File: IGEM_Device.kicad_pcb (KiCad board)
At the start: 2 copper layers, 50.2 x 47.6 mm, 28 parts, among them J1 67997-410HLF, J2 Electrode_Conn, J3 Batt_Conn, SW1 Power_Switch, U1 SaBLE-X-R2, U2 TC1014-2.85VCT713, U3 LMP91000SD_NOPB, U4 LM334MX_NOPB, U5 TPS79718QDCKRQ1, U6 G-NIMO-003

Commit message: Update to PCB and Gerber files
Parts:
- moved J2 1.91 mm to (125.1, 47.6)
- moved U3 1.91 mm to (125.1, 59.7)
- moved R1 1.42 mm to (144.8, 81.9)
- moved R2 1.42 mm to (141.6, 81.9)
- moved D1 1.27 mm to (137.2, 52.1)
- moved J3 1.27 mm to (109.9, 94.6)
- moved R5 0.64 mm to (135.9, 55.2)
- moved U4 0.64 mm to (145.4, 54.0)
- moved U1 0.64 mm to (131.4, 71.1)
- moved R3 0.63 mm to (138.4, 55.2)
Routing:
- net +2V85: track 99.5 -> 117.1 mm, vias 1 -> 3
- net /TEMP_OUT: track 29.3 -> 36.2 mm
- net +1V8: track 35.3 -> 30.8 mm
- net /EXT_TEMP_SCL: track 73.5 -> 69.7 mm
- net /IP_CONTROL: track 35.7 -> 37.5 mm
- net /JTAG_TDO: track 14.5 -> 12.9 mm
- net Net-(D1-PadA): track 6.65 -> 8.16 mm
- net +BATT: track 44.7 -> 45.7 mm
- net /EXT_TEMP_SDA: track 93.0 -> 92.1 mm
- net GND: track 212.3 -> 213.1 mm
- net /IP_CATHODE: track 8.09 -> 8.77 mm
- net /RESET: track 5.44 -> 6.08 mm
- net /JTAG_TMSC: track 4.17 -> 4.80 mm
- net /JTAG_TCXC: track 4.81 -> 5.44 mm
- net /POWER_GOOD: track 43.3 -> 44.0 mm
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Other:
- board size 50.2 x 47.6 mm -> 50.2 x 47 mm

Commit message: Minor changes
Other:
- rule via_min_size: 0.4 -> 0.5

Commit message: Minor fixes
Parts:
- removed C9: 0.1u, Capacitors_SMD:C_0805
- removed SW1: Power_Switch, footprints5:JS202011SCQN
- added C13: 100p, Capacitors_SMD:C_0805, F.Cu at (154.3, 93.3)
- added J4: Male_Data_Conn, HTSW10407GS:HTSW-104-07-G-S, F.Cu at (157.5, 54.0)
- added J5: Female_Data_Conn, 55342372:5-534237-2, B.Cu at (161.3, 83.2)
- added J6: VDD_Female_Conn, 55342371:5-534237-1, F.Cu at (141.6, 97.8)
- added J7: GND_Female_Conn, 55342371:5-534237-1, F.Cu at (173.4, 97.8)
- added J8: VDD_Male_Conn, 51462803:5-146280-3, F.Cu at (141.6, 63.5)
- added J9: GND_Male_Conn, 51462803:5-146280-3, F.Cu at (173.4, 63.5)
- added U7: ADS1100A0IDBVR, ADS1100A0TDBVR:ADS1100A0IDBVR, F.Cu at (154.3, 90.2)
- C3: moved to B.Cu
- D1: footprint SODFL1608X70N -> 1N4148WT:SODFL1608X70N
- J1: value 67997-410HLF -> M20-9980445; footprint footprints3:67997-410HLF -> M20-9980445:HDRV8W64P254_2X4_1016X508X910P
- J3: footprint footprints6:796136-1 -> S2B-PH-K-S_LF__SN_:JST_S2B-PH-K-S(LF)(SN)
- U6: moved to F.Cu
- moved R4 69.9 mm to (167.6, 83.8)
- moved U5 69.6 mm to (167.6, 86.4)
- moved C5 69.0 mm to (170.8, 83.8), turned to 270 degrees
- moved C4 68.7 mm to (170.8, 87.6), turned to 90 degrees
- moved C6 66.1 mm to (167.6, 89.5), turned to 0 degrees
- moved J2 63.5 mm to (157.5, 102.2), turned to 180 degrees
- moved U6 62.3 mm to (168.3, 96.5), turned to 270 degrees
- moved C11 52.3 mm to (142.9, 54.0)
- moved C10 50.2 mm to (170.2, 66.0), turned to 0 degrees
- moved J3 47.3 mm to (141.0, 59.1), turned to 90 degrees
- moved U3 46.8 mm to (160.7, 90.2), turned to 270 degrees
- moved D1 44.4 mm to (147.3, 95.2), turned to 180 degrees
- moved C7 44.0 mm to (170.2, 63.5), turned to 0 degrees
- moved U2 41.6 mm to (146.7, 54.0)
- moved J1 41.0 mm to (172.7, 52.7), turned to 270 degrees
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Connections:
- C12 pad 1: +3V3 -> +2V85
- C3 pad 1: Net-(C3-Pad1) -> +BATT
- J1 pad 1: +3V3 -> GND
- J1 pad 2: GND -> /RESET
- J1 pad 4: Net-(J1-Pad4) -> /JTAG_TCXC
- J1 pad 5: GND -> /JTAG_TDI
- J1 pad 6: /RESET -> /JTAG_TMSC
- J1 pad 7: /JTAG_TCXC -> /JTAG_TDO
- J1 pad 8: /JTAG_TMSC -> +2V85
- R1 pad 2: /EXT_TEMP_SDA -> /SCL
- R2 pad 2: /EXT_TEMP_SCL -> /SDA
- U1 pad 17: /IP_CONTROL -> Net-(U1-Pad17)
- U1 pad 21: /POWER_GOOD -> Net-(U1-Pad21)
- U1 pad 24: /TEMP_OUT -> Net-(U1-Pad24)
- U1 pad 29: Net-(U1-Pad29) -> /POWER_GOOD
- U1 pad 30: Net-(U1-Pad30) -> /IP_CONTROL
- U1 pad 31: /EXT_TEMP_SCL -> /SDA
- U1 pad 32: /EXT_TEMP_SDA -> /SCL
- U2 pad 1: Net-(C3-Pad1) -> +BATT
- U2 pad 3: Net-(C3-Pad1) -> +BATT
- U3 pad 3: /EXT_TEMP_SCL -> /SCL
- U3 pad 4: /EXT_TEMP_SDA -> /SDA
- U3 pad 8: /TEMP_OUT -> /LMP91000_VOUT
- U6 pad 2: /EXT_TEMP_SCL -> /SCL
- U6 pad 3: /EXT_TEMP_SDA -> /SDA
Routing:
- net /EXT_TEMP_SDA: track 92.1 -> 0.00 mm, vias 3 -> 0
- net /EXT_TEMP_SCL: track 69.7 -> 0.00 mm, vias 3 -> 0
- net /SCL: track 0.00 -> 42.2 mm, vias 0 -> 3
- net /TEMP_OUT: track 36.2 -> 0.00 mm, vias 2 -> 0
- net +BATT: track 45.7 -> 12.0 mm
- net /SDA: track 0.00 -> 32.9 mm, vias 0 -> 2
- net /POWER_GOOD: track 44.0 -> 13.4 mm, vias 2 -> 0
- net Net-(C3-Pad1): track 27.7 -> 0.00 mm
- net GND: track 213.5 -> 194.1 mm, vias 1 -> 3
- net /IP_CONTROL: track 37.5 -> 19.9 mm, vias 2 -> 0
- net /RESET: track 6.08 -> 23.1 mm, vias 0 -> 1
- net /JTAG_TCXC: track 5.44 -> 19.9 mm, vias 0 -> 1
- net /JTAG_TMSC: track 4.80 -> 16.9 mm, vias 0 -> 1
- net Net-(C1-Pad1): track 3.75 -> 12.8 mm
- net +1V8: track 30.8 -> 39.6 mm, vias 2 -> 4
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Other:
- board size 50.2 x 47 mm -> 35.6 x 47.6 mm

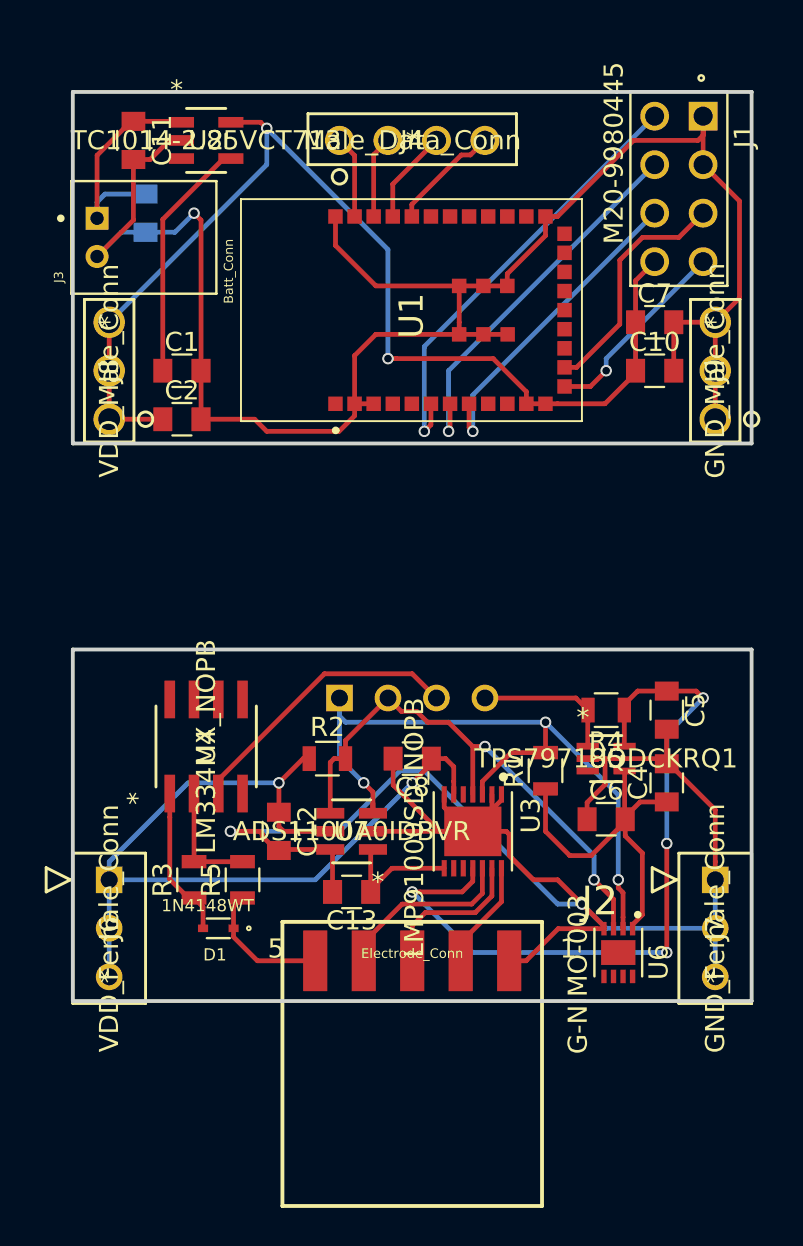
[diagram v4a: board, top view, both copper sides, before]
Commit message: Updated layout, added 3D shapes and Gerber files
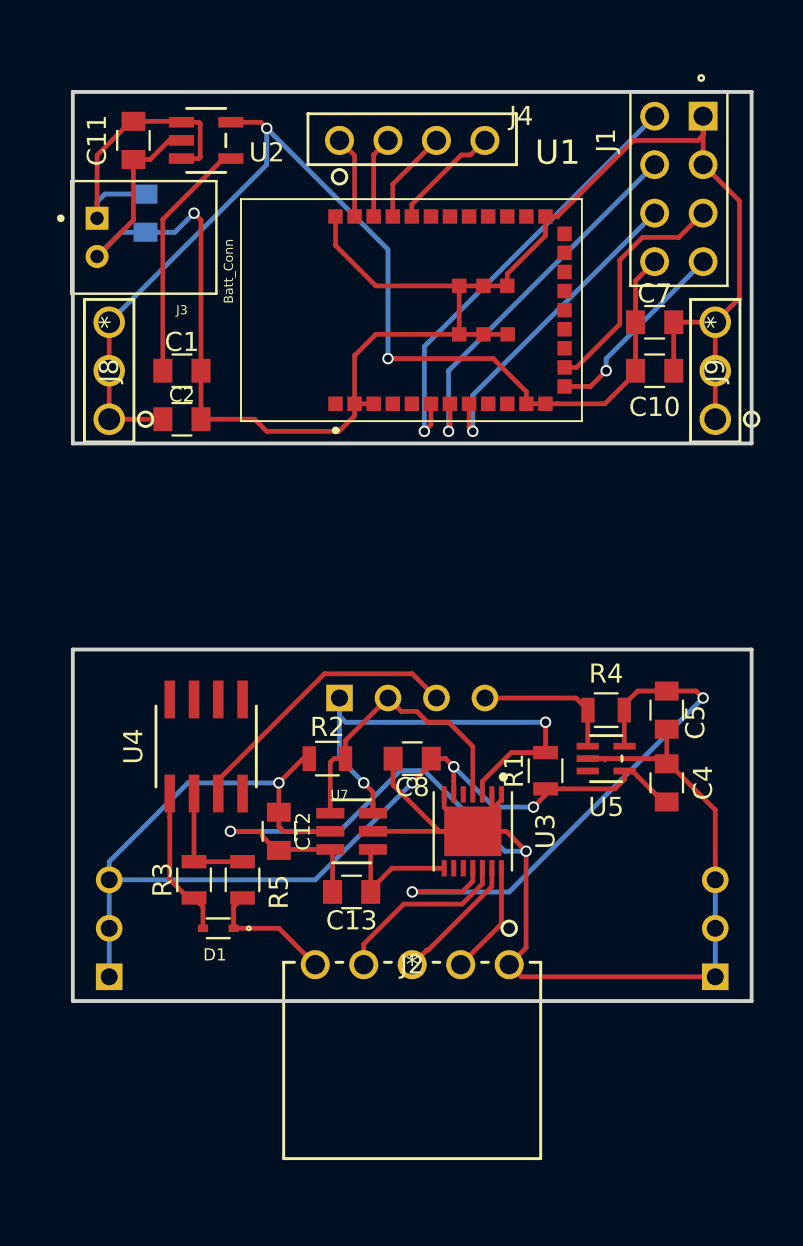
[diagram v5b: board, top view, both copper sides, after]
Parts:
- removed C6: 0.1u, Capacitors_SMD:C_0805
- removed U6: G-NIMO-003, G-NIMO-003:SON50P250X250X75-9N
- J2: footprint TSM-105-01-L-SH:TSM-105-01-L-SH -> TSW10508FSRA:TSW-105-08-F-S-RA
- J6, J7: moved to B.Cu
- moved J6 5.08 mm to (141.6, 92.7), turned to 270 degrees
- moved J7 5.08 mm to (173.4, 92.7), turned to 270 degrees
- moved J2 5.08 mm to (157.5, 97.2)
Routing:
- net /SDA: track 32.9 -> 19.9 mm, vias 2 -> 0
- net /SCL: track 42.2 -> 29.7 mm, vias 3 -> 2
- net GND: track 194.1 -> 184.2 mm
- net +1V8: track 39.6 -> 30.3 mm, vias 4 -> 2
- net +2V85: track 125.0 -> 119.6 mm, vias 4 -> 6
- net +BATT: track 12.0 -> 15.8 mm
- net /REF_ELECTRODE: track 8.11 -> 6.82 mm
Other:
- board text added: "+"
- board text added: "-"
- board text added: "C"
- board text added: "CL"
- board text added: "DA"
- board text added: "G"
- board text added: "GND"
- board text added: "I"
- board text added: "IP"
- board text added: "IPC"
- board text added: "M"
- board text added: "O"
- board text added: "PW"
- board text added: "PWG"
- board text added: "Quantifen"
- board text added: "R"
- board text added: "SCL"
- board text added: "SDA"
- board text added: "VDD"
- board text added: "W"
